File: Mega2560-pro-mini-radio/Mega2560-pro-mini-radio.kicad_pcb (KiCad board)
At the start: 2 copper layers, 64.8 x 50.8 mm, 7 parts, among them J1 COM_CONN, J2 NAV_CONN, J3 Power_Conn

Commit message: PCB de ATMega modificada para permitir conectar los switches de control de los modulos COM.
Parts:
- added J4: SW_CONN, Connector_PinSocket_2.54mm:PinSocket_2x15_P2.54mm_Horizontal, F.Cu at (160.0, 82.5)
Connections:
- J1 pad 14: Net-(J1-Pad14) -> (no net)
- J1 pad 15: Net-(J1-Pad15) -> (no net)
- J1 pad 16: Net-(J1-Pad16) -> (no net)
- J1 pad 17: Net-(J1-Pad17) -> (no net)
- J1 pad 18: Net-(J1-Pad18) -> (no net)
- J1 pad 19: Net-(J1-Pad19) -> (no net)
- J1 pad 20: Net-(J1-Pad20) -> (no net)
- J1 pad 21: Net-(J1-Pad21) -> (no net)
- J1 pad 22: Net-(J1-Pad22) -> (no net)
- J1 pad 23: Net-(J1-Pad23) -> (no net)
- J1 pad 24: Net-(J1-Pad24) -> (no net)
- J1 pad 25: Net-(J1-Pad25) -> (no net)
- J1 pad 26: Net-(J1-Pad26) -> (no net)
- J1 pad 27: Net-(J1-Pad27) -> (no net)
- J1 pad 28: Net-(J1-Pad28) -> (no net)
- J1 pad 29: Net-(J1-Pad29) -> (no net)
- J1 pad 5: Net-(J1-Pad5) -> (no net)
- J2 pad 13: Net-(J2-Pad13) -> (no net)
- J2 pad 14: Net-(J2-Pad14) -> (no net)
- J2 pad 15: Net-(J2-Pad15) -> (no net)
- J2 pad 16: Net-(J2-Pad16) -> (no net)
- J2 pad 17: Net-(J2-Pad17) -> (no net)
- J2 pad 18: Net-(J2-Pad18) -> (no net)
- J2 pad 19: Net-(J2-Pad19) -> (no net)
- J2 pad 20: Net-(J2-Pad20) -> (no net)
- J2 pad 21: Net-(J2-Pad21) -> (no net)
- J2 pad 22: Net-(J2-Pad22) -> (no net)
- J2 pad 23: Net-(J2-Pad23) -> (no net)
- J2 pad 24: Net-(J2-Pad24) -> (no net)
- J2 pad 25: Net-(J2-Pad25) -> (no net)
- J2 pad 26: Net-(J2-Pad26) -> (no net)
- J2 pad 27: Net-(J2-Pad27) -> (no net)
- J2 pad 28: Net-(J2-Pad28) -> (no net)
- J2 pad 29: Net-(J2-Pad29) -> (no net)
- J2 pad 5: Net-(J2-Pad5) -> (no net)
- MCU1 pad 10: Net-(MCU1-Pad10) -> (no net)
- MCU1 pad 11: Net-(MCU1-Pad11) -> (no net)
- MCU1 pad 12: Net-(MCU1-Pad12) -> (no net)
- MCU1 pad 13: Net-(MCU1-Pad13) -> (no net)
- MCU1 pad 14: Net-(MCU1-Pad14) -> (no net)
- MCU1 pad 15: Net-(MCU1-Pad15) -> (no net)
- MCU1 pad 16: Net-(MCU1-Pad16) -> (no net)
- MCU1 pad 17: Net-(MCU1-Pad17) -> (no net)
- MCU1 pad 18: Net-(MCU1-Pad18) -> (no net)
- MCU1 pad 19: Net-(MCU1-Pad19) -> (no net)
- MCU1 pad 20: Net-(MCU1-Pad20) -> (no net)
- MCU1 pad 21: Net-(MCU1-Pad21) -> (no net)
- MCU1 pad 33: Net-(MCU1-Pad33) -> (no net)
- MCU1 pad 40: Net-(MCU1-Pad40) -> COM1
- MCU1 pad 41: Net-(MCU1-Pad41) -> COM2
- MCU1 pad 42: Net-(MCU1-Pad42) -> BOTH
- MCU1 pad 43: Net-(MCU1-Pad43) -> (no net)
- MCU1 pad 44: Net-(MCU1-Pad44) -> (no net)
- MCU1 pad 45: Net-(MCU1-Pad45) -> (no net)
- MCU1 pad 46: Net-(MCU1-Pad46) -> (no net)
- MCU1 pad 47: Net-(MCU1-Pad47) -> (no net)
- MCU1 pad 48: Net-(MCU1-Pad48) -> (no net)
- MCU1 pad 49: Net-(MCU1-Pad49) -> NAV1
- MCU1 pad 50: Net-(MCU1-Pad50) -> NAV2
- MCU1 pad 51: Net-(MCU1-Pad51) -> MKR
- MCU1 pad 52: Net-(MCU1-Pad52) -> DME
- MCU1 pad 53: Net-(MCU1-Pad53) -> ADF
- MCU1 pad 54: Net-(MCU1-Pad54) -> AUX
- MCU1 pad 55: Net-(MCU1-Pad55) -> O_led
- MCU1 pad 56: Net-(MCU1-Pad56) -> M_led
- MCU1 pad 57: Net-(MCU1-Pad57) -> I_led
- MCU1 pad 58: Net-(MCU1-Pad58) -> (no net)
- MCU1 pad 59: Net-(MCU1-Pad59) -> (no net)
- MCU1 pad 60: Net-(MCU1-Pad60) -> (no net)
- MCU1 pad 61: Net-(MCU1-Pad61) -> (no net)
- MCU1 pad 62: Net-(MCU1-Pad62) -> (no net)
- MCU1 pad 63: Net-(MCU1-Pad63) -> (no net)
- MCU1 pad 64: Net-(MCU1-Pad64) -> (no net)
- MCU1 pad 65: Net-(MCU1-Pad65) -> (no net)
- MCU1 pad 66: Net-(MCU1-Pad66) -> (no net)
- MCU1 pad 67: Net-(MCU1-Pad67) -> (no net)
- MCU1 pad 68: Net-(MCU1-Pad68) -> (no net)
- MCU1 pad 69: Net-(MCU1-Pad69) -> (no net)
- MCU1 pad 7: Net-(MCU1-Pad7) -> (no net)
- MCU1 pad 70: Net-(MCU1-Pad70) -> (no net)
- MCU1 pad 71: Net-(MCU1-Pad71) -> (no net)
- MCU1 pad 72: Net-(MCU1-Pad72) -> (no net)
- MCU1 pad 73: Net-(MCU1-Pad73) -> (no net)
- MCU1 pad 74: Net-(MCU1-Pad74) -> (no net)
- MCU1 pad 75: Net-(MCU1-Pad75) -> (no net)
- MCU1 pad 76: Net-(MCU1-Pad76) -> (no net)
- MCU1 pad 77: Net-(MCU1-Pad77) -> (no net)
- MCU1 pad 78: Net-(MCU1-Pad78) -> (no net)
- MCU1 pad 79: Net-(MCU1-Pad79) -> (no net)
- MCU1 pad 8: Net-(MCU1-Pad8) -> (no net)
- MCU1 pad 80: Net-(MCU1-Pad80) -> (no net)
- MCU1 pad 81: Net-(MCU1-Pad81) -> (no net)
- MCU1 pad 82: Net-(MCU1-Pad82) -> (no net)
- MCU1 pad 83: Net-(MCU1-Pad83) -> (no net)
- MCU1 pad 84: Net-(MCU1-Pad84) -> (no net)
- MCU1 pad 85: Net-(MCU1-Pad85) -> (no net)
- MCU1 pad 86: Net-(MCU1-Pad86) -> (no net)
- MCU1 pad 9: Net-(MCU1-Pad9) -> (no net)
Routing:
- net +5V: track 67.2 -> 135.9 mm
- net COM1: track 0.00 -> 53.8 mm
- net GND: track 120.8 -> 170.0 mm
- net BOTH: track 0.00 -> 46.1 mm
- net COM2: track 0.00 -> 39.9 mm
- net NAV2: track 0.00 -> 26.1 mm
- net NAV1: track 0.00 -> 24.1 mm
- net MKR: track 0.00 -> 23.3 mm
- net DME: track 0.00 -> 23.1 mm
- net I_led: track 0.00 -> 19.2 mm
- net SW_NAV_ENC_KHZ: track 31.0 -> 17.4 mm
- net B_COM_ENC_KHZ: track 48.4 -> 35.1 mm, vias 0 -> 2
- net M_led: track 0.00 -> 12.9 mm
- net AUX: track 0.00 -> 11.9 mm
- net A_COM_ENC_MHZ: track 41.1 -> 49.0 mm
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- removed copper zone on B.Cu, net GND
- removed copper zone on F.Cu, net GND
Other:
- board size 64.8 x 50.8 mm -> 64.8 x 59.7 mm

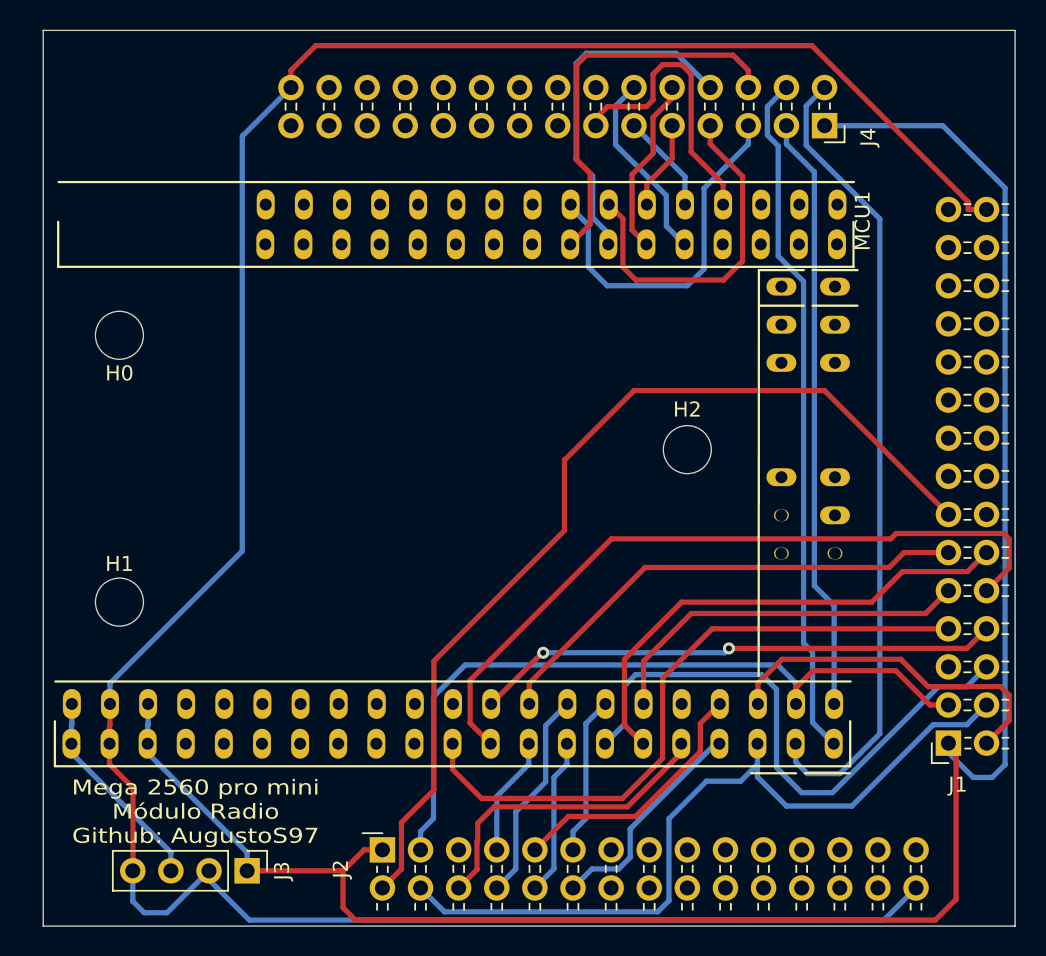
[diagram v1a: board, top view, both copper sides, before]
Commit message: Añadidos los soportes para ATMega.
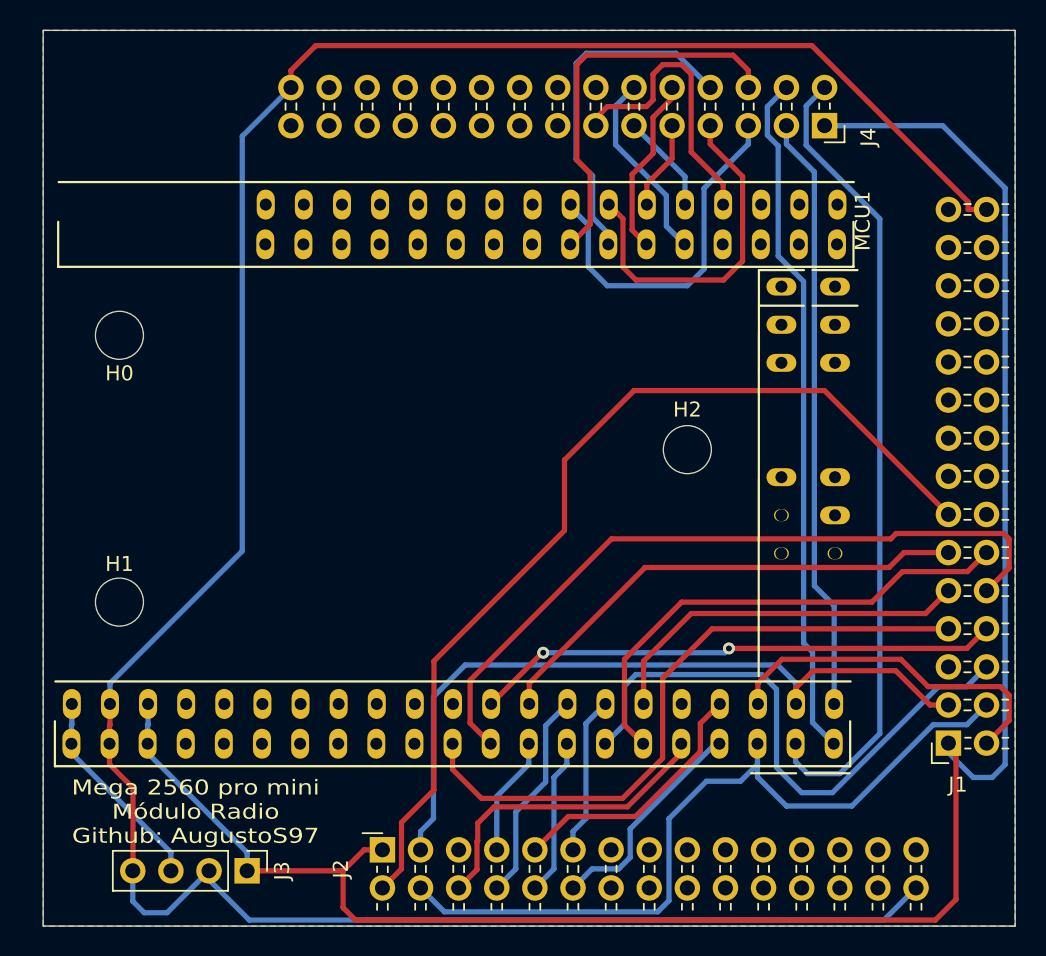
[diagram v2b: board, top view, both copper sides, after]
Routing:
- added copper zone on B.Cu, net GND
- added copper zone on F.Cu, net GND
